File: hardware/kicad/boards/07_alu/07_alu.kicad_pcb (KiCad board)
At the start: 2 copper layers, 104 parts, among them J1 Conn_01x08_Pin, J2 Conn_01x08_Pin, J3 Conn_01x08_Pin, J4 Conn_01x08_Pin, J5 Conn_01x08_Pin, J6 Conn_01x08_Pin, J7 Conn_01x16, SW1 SW_Slide_DPDT, U1 74ACT151, U10 74ACT151, U11 74ACT151, U12 74ACT151, U13 74ACT151, U14 74ACT151, U15 74ACT283, U16 74LS32, U17 74ACT151, U18 74ACT151, U19 74ACT151, U2 74ACT151, U20 74ACT151, U21 74ACT151, U22 74ACT151, U23 74ACT151, U24 74ACT151, U25 74ACT283, U26 74LS32, U27 74ACT151, U28 74ACT151, U29 74ACT151, U3 74ACT283, U30 74ACT151, U31 74ACT151, U32 74ACT151, U33 74ACT151, U34 74ACT151, U35 SST39SF040, U36 SST39SF040, U37 74AHC541, U38 74AHC541, U39 SST39SF040, U4 74LS32, U40 74AHC541, U41 74ACT151, U42 74ACT151, U43 74ACT151, U44 74ACT151, U45 74ACT151, U46 74ACT151, U47 74ACT151, U48 74ACT151, U5 74ACT283, U6 74LS32, U7 74ACT151, U8 74ACT151, U9 74ACT151

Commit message: checkpoint: most recent 16b cell: ~120mm by 120mm
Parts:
- removed C1, C10, C11, C12, C13, C14, C15, C17, C18, C19, C2, C20, C21, C22, C23, C24, C25, C26, C27, C28, C29, C30, C31, C32, C33, C34, C35, C38, C7, C8, C9: 100nF, Capacitor_SMD:C_0603_1608Metric
- removed SW1: SW_Slide_DPDT, Button_Switch_SMD:SW_DPDT_CK_JS202011JCQN
- removed U1, U10, U11, U12, U13, U14, U17, U18, U19, U2, U20, U21, U22, U23, U24, U27, U28, U29, U30, U31, U32, U33, U34, U9: 74ACT151, Package_SO:SOIC-16_3.9x9.9mm_P1.27mm
- removed U15, U25: 74ACT283, Package_SO:SOIC-16_3.9x9.9mm_P1.27mm
- removed U26: 74LS32, Package_SO:SOIC-14_3.9x8.7mm_P1.27mm
- removed U35, U39: SST39SF040, Package_DIP:DIP-32_W15.24mm
- added C49: 100nF, Capacitor_SMD:C_0603_1608Metric, F.Cu at (57.5, 41.8)
- added C50: 100nF, Capacitor_SMD:C_0603_1608Metric, F.Cu at (57.5, 44.3)
- added C51: 100nF, Capacitor_SMD:C_0603_1608Metric, F.Cu at (132.9, 125.5)
- added C52: 100nF, Capacitor_SMD:C_0603_1608Metric, F.Cu at (118.4, 125.5)
- added C53: 100nF, Capacitor_SMD:C_0603_1608Metric, F.Cu at (132.9, 111.8)
- added C54: 100nF, Capacitor_SMD:C_0603_1608Metric, F.Cu at (147.4, 98.2)
- added C55: 100nF, Capacitor_SMD:C_0603_1608Metric, F.Cu at (147.4, 111.8)
- added C56: 100nF, Capacitor_SMD:C_0603_1608Metric, F.Cu at (118.4, 111.8)
- added C57: 100nF, Capacitor_SMD:C_0603_1608Metric, F.Cu at (132.9, 98.2)
- added C58: 100nF, Capacitor_SMD:C_0603_1608Metric, F.Cu at (161.8, 98.2)
- added C59: 100nF, Capacitor_SMD:C_0603_1608Metric, F.Cu at (132.9, 84.6)
- added C60: 100nF, Capacitor_SMD:C_0603_1608Metric, F.Cu at (118.4, 71.0)
- added C61: 100nF, Capacitor_SMD:C_0603_1608Metric, F.Cu at (118.4, 84.6)
- added C62: 100nF, Capacitor_SMD:C_0603_1608Metric, F.Cu at (147.4, 71.0)
- added C63: 100nF, Capacitor_SMD:C_0603_1608Metric, F.Cu at (161.8, 84.6)
- added C64: 100nF, Capacitor_SMD:C_0603_1608Metric, F.Cu at (161.8, 57.4)
- added C65: 100nF, Capacitor_SMD:C_0603_1608Metric, F.Cu at (132.9, 71.0)
- added C66: 100nF, Capacitor_SMD:C_0603_1608Metric, F.Cu at (161.8, 71.0)
- added C67: 100nF, Capacitor_SMD:C_0603_1608Metric, F.Cu at (118.4, 57.4)
- added C68: 100nF, Capacitor_SMD:C_0603_1608Metric, F.Cu at (66.0, 130.8)
- added C69: 100nF, Capacitor_SMD:C_0603_1608Metric, F.Cu at (94.9, 130.8)
- added C70: 100nF, Capacitor_SMD:C_0603_1608Metric, F.Cu at (80.4, 130.8)
- added C71: 100nF, Capacitor_SMD:C_0603_1608Metric, F.Cu at (132.9, 57.4)
- added C72: 100nF, Capacitor_SMD:C_0603_1608Metric, F.Cu at (66.0, 117.2)
- added C73: 100nF, Capacitor_SMD:C_0603_1608Metric, F.Cu at (80.4, 117.2)
- added C74: 100nF, Capacitor_SMD:C_0603_1608Metric, F.Cu at (94.9, 117.2)
- added D1: LED, LED_SMD:LED_0805_2012Metric, F.Cu at (158.8, 29.5)
- added D10: LED, LED_SMD:LED_0805_2012Metric, F.Cu at (57.7, 103.3)
- added D11: LED, LED_SMD:LED_0805_2012Metric, F.Cu at (57.7, 106.4)
- added D12: LED, LED_SMD:LED_0805_2012Metric, F.Cu at (57.7, 109.4)
- added D13: LED, LED_SMD:LED_0805_2012Metric, F.Cu at (57.7, 112.4)
- added D14: LED, LED_SMD:LED_0805_2012Metric, F.Cu at (62.2, 94.2)
- added D15: LED, LED_SMD:LED_0805_2012Metric, F.Cu at (62.2, 97.2)
- added D16: LED, LED_SMD:LED_0805_2012Metric, F.Cu at (62.2, 100.3)
- added D17: LED, LED_SMD:LED_0805_2012Metric, F.Cu at (62.2, 103.3)
- added D18: LED, LED_SMD:LED_0805_2012Metric, F.Cu at (62.2, 106.4)
- added D19: LED, LED_SMD:LED_0805_2012Metric, F.Cu at (62.2, 109.4)
- added D20: LED, LED_SMD:LED_0805_2012Metric, F.Cu at (62.2, 112.4)
- added D21: LED, LED_SMD:LED_0805_2012Metric, F.Cu at (66.6, 94.2)
- added D22: LED, LED_SMD:LED_0805_2012Metric, F.Cu at (66.6, 97.2)
- added D23: LED, LED_SMD:LED_0805_2012Metric, F.Cu at (66.6, 100.3)
- added D24: LED, LED_SMD:LED_0805_2012Metric, F.Cu at (66.6, 103.3)
- added D25: LED, LED_SMD:LED_0805_2012Metric, F.Cu at (66.6, 106.4)
- added D26: LED, LED_SMD:LED_0805_2012Metric, F.Cu at (66.6, 109.4)
- added D27: LED, LED_SMD:LED_0805_2012Metric, F.Cu at (66.6, 112.4)
- added D28: LED, LED_SMD:LED_0805_2012Metric, F.Cu at (71.1, 94.2)
- added D29: LED, LED_SMD:LED_0805_2012Metric, F.Cu at (71.1, 97.2)
- added D3: LED, LED_SMD:LED_0805_2012Metric, F.Cu at (57.7, 94.2)
- added D30: LED, LED_SMD:LED_0805_2012Metric, F.Cu at (71.1, 100.3)
- added D31: LED, LED_SMD:LED_0805_2012Metric, F.Cu at (71.1, 103.3)
- added D32: LED, LED_SMD:LED_0805_2012Metric, F.Cu at (71.1, 106.4)
- added D4: LED, LED_SMD:LED_0805_2012Metric, F.Cu at (57.7, 97.2)
- added D9: LED, LED_SMD:LED_0805_2012Metric, F.Cu at (57.7, 100.3)
- added J10: Conn_01x04_Pin, Connector_PinHeader_2.54mm:PinHeader_1x04_P2.54mm_Vertical, F.Cu at (57.8, 80.8)
- added J11: Conn_01x04_Pin, Connector_PinHeader_2.54mm:PinHeader_1x04_P2.54mm_Vertical, F.Cu at (62.4, 80.8)
- added J12: Conn_01x08_Pin, Connector_PinHeader_2.54mm:PinHeader_1x08_P2.54mm_Vertical, F.Cu at (99.1, 58.4)
- added J13: Conn_01x08_Pin, Connector_PinHeader_2.54mm:PinHeader_1x08_P2.54mm_Vertical, F.Cu at (103.7, 58.4)
- added J8: Conn_01x08_Pin, Connector_PinHeader_2.54mm:PinHeader_1x08_P2.54mm_Vertical, F.Cu at (89.9, 58.4)
- added J9: Conn_01x08_Pin, Connector_PinHeader_2.54mm:PinHeader_1x08_P2.54mm_Vertical, F.Cu at (94.5, 58.4)
- added R1: 330 Ohm, Resistor_SMD:R_0603_1608Metric, F.Cu at (158.5, 32.3)
- added R10: 330, Resistor_SMD:R_0603_1608Metric, F.Cu at (75.3, 101.5)
- added R11: 330, Resistor_SMD:R_0603_1608Metric, F.Cu at (75.3, 104.0)
- added R12: 330, Resistor_SMD:R_0603_1608Metric, F.Cu at (75.3, 106.5)
- added R13: 330, Resistor_SMD:R_0603_1608Metric, F.Cu at (75.3, 109.0)
- added R14: 330, Resistor_SMD:R_0603_1608Metric, F.Cu at (79.3, 93.9)
- added R15: 330, Resistor_SMD:R_0603_1608Metric, F.Cu at (79.3, 96.4)
- added R16: 330, Resistor_SMD:R_0603_1608Metric, F.Cu at (79.3, 99.0)
- added R17: 330, Resistor_SMD:R_0603_1608Metric, F.Cu at (79.3, 101.5)
- added R18: 330, Resistor_SMD:R_0603_1608Metric, F.Cu at (79.3, 104.0)
- added R19: 330, Resistor_SMD:R_0603_1608Metric, F.Cu at (79.3, 106.5)
- added R20: 330, Resistor_SMD:R_0603_1608Metric, F.Cu at (79.3, 109.0)
- added R21: 330, Resistor_SMD:R_0603_1608Metric, F.Cu at (83.3, 93.9)
- added R22: 330, Resistor_SMD:R_0603_1608Metric, F.Cu at (83.3, 96.4)
- added R23: 330, Resistor_SMD:R_0603_1608Metric, F.Cu at (83.3, 99.0)
- added R24: 330, Resistor_SMD:R_0603_1608Metric, F.Cu at (83.3, 101.5)
- added R25: 330, Resistor_SMD:R_0603_1608Metric, F.Cu at (83.3, 104.0)
- added R26: 330, Resistor_SMD:R_0603_1608Metric, F.Cu at (83.3, 106.5)
- added R27: 330, Resistor_SMD:R_0603_1608Metric, F.Cu at (83.3, 109.0)
- added R28: 330, Resistor_SMD:R_0603_1608Metric, F.Cu at (87.3, 93.9)
- added R29: 330, Resistor_SMD:R_0603_1608Metric, F.Cu at (87.3, 96.4)
- added R3: 330 Ohm, Resistor_SMD:R_0603_1608Metric, F.Cu at (75.3, 93.9)
- added R30: 330, Resistor_SMD:R_0603_1608Metric, F.Cu at (87.3, 99.0)
- added R31: 330, Resistor_SMD:R_0603_1608Metric, F.Cu at (87.3, 101.5)
- added R4: 330, Resistor_SMD:R_0603_1608Metric, F.Cu at (75.3, 96.4)
- added R9: 330, Resistor_SMD:R_0603_1608Metric, F.Cu at (75.3, 99.0)
- added U49: 74ACT151, Package_SO:SOIC-16_3.9x9.9mm_P1.27mm, F.Cu at (141.1, 102.9)
- added U50: 74ACT151, Package_SO:SOIC-16_3.9x9.9mm_P1.27mm, F.Cu at (126.7, 130.1)
- added U51: 74ACT151, Package_SO:SOIC-16_3.9x9.9mm_P1.27mm, F.Cu at (112.2, 130.1)
- added U52: 74ACT151, Package_SO:SOIC-16_3.9x9.9mm_P1.27mm, F.Cu at (126.7, 116.5)
- added U53: 74ACT151, Package_SO:SOIC-16_3.9x9.9mm_P1.27mm, F.Cu at (141.1, 116.5)
- added U54: 74ACT151, Package_SO:SOIC-16_3.9x9.9mm_P1.27mm, F.Cu at (126.7, 102.9)
- added U55: 74ACT151, Package_SO:SOIC-16_3.9x9.9mm_P1.27mm, F.Cu at (155.6, 102.9)
- added U56: 74ACT151, Package_SO:SOIC-16_3.9x9.9mm_P1.27mm, F.Cu at (112.2, 116.5)
- added U57: 74ACT151, Package_SO:SOIC-16_3.9x9.9mm_P1.27mm, F.Cu at (141.1, 75.6)
- added U58: 74ACT151, Package_SO:SOIC-16_3.9x9.9mm_P1.27mm, F.Cu at (126.7, 89.2)
- added U59: 74ACT151, Package_SO:SOIC-16_3.9x9.9mm_P1.27mm, F.Cu at (112.2, 75.6)
- added U60: 74ACT151, Package_SO:SOIC-16_3.9x9.9mm_P1.27mm, F.Cu at (112.2, 89.2)
- added U61: 74ACT151, Package_SO:SOIC-16_3.9x9.9mm_P1.27mm, F.Cu at (155.6, 89.2)
- added U62: 74ACT151, Package_SO:SOIC-16_3.9x9.9mm_P1.27mm, F.Cu at (126.7, 75.6)
- added U63: 74ACT151, Package_SO:SOIC-16_3.9x9.9mm_P1.27mm, F.Cu at (155.6, 75.6)
- added U64: 74ACT151, Package_SO:SOIC-16_3.9x9.9mm_P1.27mm, F.Cu at (155.6, 62.0)
- added U65: 74ACT151, Package_SO:SOIC-16_3.9x9.9mm_P1.27mm, F.Cu at (74.2, 135.5)
- added U66: 74ACT151, Package_SO:SOIC-16_3.9x9.9mm_P1.27mm, F.Cu at (112.2, 62.0)
- added U67: 74ACT151, Package_SO:SOIC-16_3.9x9.9mm_P1.27mm, F.Cu at (59.7, 135.5)
- added U68: 74ACT151, Package_SO:SOIC-16_3.9x9.9mm_P1.27mm, F.Cu at (88.6, 135.5)
- added U69: 74ACT151, Package_SO:SOIC-16_3.9x9.9mm_P1.27mm, F.Cu at (126.7, 62.0)
- added U70: 74ACT151, Package_SO:SOIC-16_3.9x9.9mm_P1.27mm, F.Cu at (74.2, 121.9)
- added U71: 74ACT151, Package_SO:SOIC-16_3.9x9.9mm_P1.27mm, F.Cu at (88.6, 121.9)
- added U72: 74ACT151, Package_SO:SOIC-16_3.9x9.9mm_P1.27mm, F.Cu at (59.7, 121.9)
- J7: value Conn_01x16 -> Conn_01x08_Pin; footprint Connector_PinHeader_2.54mm:PinHeader_1x16_P2.54mm_Vertical -> Connector_PinHeader_2.54mm:PinHeader_1x08_P2.54mm_Vertical
- U16: value 74LS32 -> 74ACT151; footprint Package_SO:SOIC-14_3.9x8.7mm_P1.27mm -> Package_SO:SOIC-16_3.9x9.9mm_P1.27mm
- U36: value SST39SF040 -> 74HC86; footprint Package_DIP:DIP-32_W15.24mm -> Package_SO:SOIC-14_3.9x8.7mm_P1.27mm
- U37: value 74AHC541 -> 74LS08; footprint Package_SO:SOIC-20W_7.5x12.8mm_P1.27mm -> Package_SO:SOIC-14_3.9x8.7mm_P1.27mm
- U38: value 74AHC541 -> 74LS540
- U4, U6: value 74LS32 -> 74HC688; footprint Package_SO:SOIC-14_3.9x8.7mm_P1.27mm -> Package_SO:SOIC-20W_7.5x12.8mm_P1.27mm
- U40: value 74AHC541 -> 74LS377
- U7, U8: value 74ACT151 -> 74ACT283
- moved U4 100.0 mm to (66.0, 35.3)
- moved C44 91.6 mm to (138.1, 29.3)
- moved C45 91.6 mm to (152.5, 29.3)
- moved C47 91.6 mm to (138.1, 42.9)
- moved U44 91.6 mm to (131.8, 33.9)
- moved U45 91.6 mm to (146.3, 33.9)
- moved U47 91.6 mm to (131.8, 47.5)
- moved C16 87.5 mm to (57.5, 29.3)
- moved U43 82.0 mm to (117.4, 33.9)
- moved C43 82.0 mm to (123.6, 29.3)
- moved U6 80.1 mm to (78.9, 35.3)
- moved C48 76.5 mm to (123.6, 42.9)
- moved U48 76.5 mm to (117.4, 47.5)
- moved U5 75.4 mm to (112.2, 102.9)
- moved C6 72.8 mm to (101.8, 93.9)
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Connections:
- C36 pad 1: VCC -> GND
- C36 pad 2: GND -> VCC
- C37 pad 1: VCC -> GND
- C37 pad 2: GND -> VCC
- C39 pad 1: VCC -> GND
- C39 pad 2: GND -> VCC
- J7 pad 1: OPCODE0 -> ALU_OPCODE_Y0
- J7 pad 2: OPCODE1 -> ALU_OPCODE_Y1
- J7 pad 3: OPCODE2 -> ALU_OPCODE_Y2
- J7 pad 4: OPCODE3 -> ALU_OPCODE_Y3
- J7 pad 5: OPCODE4 -> ALU_OPCODE_Y4
- J7 pad 6: OPCODE5 -> ALU_OPCODE_Y5
- J7 pad 7: OPCODE6 -> ALU_OPCODE_Y6
- J7 pad 8: OPCODE7 -> ALU_OPCODE_Y7
- U16 pad 1: OUT8 -> flagZ
- U16 pad 10: Net-(U16-Pad10) -> CSEL1
- U16 pad 11: /alu_4b_2/Z_out -> CSEL0
- U16 pad 12: Net-(U16-Pad12) -> flagGT
- U16 pad 13: /alu_4b_1/Z_out -> flagLT
- U16 pad 14: VCC -> flagV
- U16 pad 2: OUT9 -> flagC
- U16 pad 3: Net-(U16-Pad3) -> VCC
- U16 pad 4: OUT10 -> GND
- U16 pad 5: OUT11 -> CIN-MAIN
- U16 pad 6: Net-(U16-Pad10) -> unconnected-(U16-~{Z}-Pad6)
- U16 pad 8: Net-(U16-Pad12) -> GND
- U16 pad 9: Net-(U16-Pad3) -> CSEL2
- U3 pad 7: CIN -> CIN-MAIN
- U36 pad 1: GND -> Aeff
- U36 pad 10: OPCODE2 -> VOUT
- U36 pad 11: OPCODE1 -> unconnected-(U36-Pad11)
- U36 pad 12: OPCODE0 -> unconnected-(U36-Pad12)
- U36 pad 13: Net-(U36-D0) -> unconnected-(U36-Pad13)
- U36 pad 14: Net-(U36-D1) -> VCC
- U36 pad 2: GND -> sum15
- U36 pad 3: OPCODE15 -> Net-(U36-Pad3)
- U36 pad 4: OPCODE12 -> sum15
- U36 pad 5: OPCODE7 -> Beff
- U36 pad 6: OPCODE6 -> Net-(U36-Pad6)
- U36 pad 7: OPCODE5 -> GND
- U36 pad 8: OPCODE4 -> LT-SIGN
- U36 pad 9: OPCODE3 -> OUT15
- U37 pad 1: GND -> Net-(U36-Pad3)
- U37 pad 10: GND -> unconnected-(U37-Pad10)
- U37 pad 11: CTRL2 -> GT-SIGN
- U37 pad 12: CTRL1 -> GTE-SIGN
- U37 pad 13: CTRL0 -> ~ZOUT
- U37 pad 14: FLAG_WE -> VCC
- U37 pad 2: Net-(U36-D0) -> Net-(U36-Pad6)
- U37 pad 3: Net-(U36-D1) -> VOUT
- U37 pad 4: Net-(U36-D2) -> unconnected-(U37-Pad4)
- U37 pad 5: Net-(U36-D3) -> unconnected-(U37-Pad5)
- U37 pad 6: Net-(U36-D4) -> unconnected-(U37-Pad6)
- U37 pad 7: Net-(U36-D5) -> GND
- U37 pad 8: Net-(U36-D6) -> unconnected-(U37-Pad8)
- U37 pad 9: Net-(U36-D7) -> unconnected-(U37-Pad9)
- U38 pad 11: ALU_OPCODE_X7 -> unconnected-(U38-Y7-Pad11)
- U38 pad 12: ALU_OPCODE_X6 -> unconnected-(U38-Y6-Pad12)
- U38 pad 13: ALU_OPCODE_X5 -> ~flagWE
- U38 pad 14: ALU_OPCODE_X4 -> unconnected-(U38-Y4-Pad14)
- U38 pad 15: ALU_OPCODE_X3 -> GTE-SIGN
- U38 pad 16: ALU_OPCODE_X2 -> unconnected-(U38-Y2-Pad16)
- U38 pad 17: ALU_OPCODE_X1 -> unconnected-(U38-Y1-Pad17)
- U38 pad 18: ALU_OPCODE_X0 -> ZOUT
- U38 pad 2: Net-(U35-D0) -> ~ZOUT
- U38 pad 3: Net-(U35-D1) -> unconnected-(U38-A1-Pad3)
- U38 pad 4: Net-(U35-D2) -> VOUT
- U38 pad 5: Net-(U35-D3) -> LT-SIGN
- U38 pad 6: Net-(U35-D4) -> OUT15
- U38 pad 7: Net-(U35-D5) -> FLAG_WE
- U38 pad 8: Net-(U35-D6) -> unconnected-(U38-A6-Pad8)
- U38 pad 9: Net-(U35-D7) -> unconnected-(U38-A7-Pad9)
- U4 pad 1: OUT0 -> GND
- U4 pad 10: Net-(U4-Pad10) -> GND
- U4 pad 11: /alu_4b_0/Z_out -> OUT4
- U4 pad 12: Net-(U4-Pad12) -> GND
- U4 pad 13: /alu_4b_0/Z_in -> OUT5
- U4 pad 14: VCC -> GND
- U4 pad 2: OUT1 -> OUT0
- U4 pad 3: Net-(U4-Pad3) -> GND
- U4 pad 4: OUT2 -> OUT1
- U4 pad 5: OUT3 -> GND
- U4 pad 6: Net-(U4-Pad10) -> OUT2
- U4 pad 8: Net-(U4-Pad12) -> OUT3
- U4 pad 9: Net-(U4-Pad3) -> GND
- U40 pad 1: GND -> ~flagWE
- U40 pad 11: ALU_OPCODE_Y7 -> SYS-CLK
- U40 pad 12: ALU_OPCODE_Y6 -> flagV
- U40 pad 13: ALU_OPCODE_Y5 -> VOUT
- U40 pad 14: ALU_OPCODE_Y4 -> LT-SIGN
- U40 pad 15: ALU_OPCODE_Y3 -> flagLT
- U40 pad 16: ALU_OPCODE_Y2 -> flagGT
- U40 pad 17: ALU_OPCODE_Y1 -> GT-SIGN
- U40 pad 18: ALU_OPCODE_Y0 -> GTE-SIGN
- U40 pad 19: GND -> flagGTE
- U40 pad 2: Net-(U39-D0) -> flagZ
- U40 pad 3: Net-(U39-D1) -> ZOUT
- U40 pad 4: Net-(U39-D2) -> ~ZOUT
- U40 pad 5: Net-(U39-D3) -> ~flagZ
- U40 pad 6: Net-(U39-D4) -> flagN
- U40 pad 7: Net-(U39-D5) -> OUT15
- U40 pad 8: Net-(U39-D6) -> COUT-MAIN
- U40 pad 9: Net-(U39-D7) -> flagC
- U6 pad 1: OUT4 -> Net-(U4-P=R)
- U6 pad 10: Net-(U6-Pad10) -> GND
- U6 pad 11: /alu_4b_1/Z_out -> OUT12
- U6 pad 12: Net-(U6-Pad12) -> GND
- U6 pad 13: /alu_4b_0/Z_out -> OUT13
- U6 pad 14: VCC -> GND
- U6 pad 2: OUT5 -> OUT8
- U6 pad 3: Net-(U6-Pad3) -> GND
- U6 pad 4: OUT6 -> OUT9
- U6 pad 5: OUT7 -> GND
- U6 pad 6: Net-(U6-Pad10) -> OUT10
- U6 pad 8: Net-(U6-Pad12) -> OUT11
- U6 pad 9: Net-(U6-Pad3) -> GND
- U7 pad 1: ALU_OPCODE_X3 -> OUT9
- U7 pad 10: B4 -> OUT11
- U7 pad 11: A4 -> /alu_4b_2/logB3
- U7 pad 12: ALU_OPCODE_X7 -> /alu_4b_2/logA3
- U7 pad 13: ALU_OPCODE_X6 -> OUT10
- U7 pad 14: ALU_OPCODE_X5 -> /alu_4b_2/logA2
- U7 pad 15: ALU_OPCODE_X4 -> /alu_4b_2/logB2
- U7 pad 2: ALU_OPCODE_X2 -> /alu_4b_2/logB1
- U7 pad 3: ALU_OPCODE_X1 -> /alu_4b_2/logA1
- U7 pad 4: ALU_OPCODE_X0 -> OUT8
- U7 pad 5: /alu_4b_1/logA0 -> /alu_4b_2/logA0
- U7 pad 6: unconnected-(U7-~{Z}-Pad6) -> /alu_4b_2/logB0
- U7 pad 7: GND -> /alu_4b_1/cout
- U7 pad 9: C4 -> /alu_4b_2/cout
- U8 pad 1: ALU_OPCODE_X3 -> OUT13
- U8 pad 10: B5 -> sum15
- U8 pad 11: A5 -> Beff
- U8 pad 12: ALU_OPCODE_X7 -> Aeff
- U8 pad 13: ALU_OPCODE_X6 -> OUT14
- U8 pad 14: ALU_OPCODE_X5 -> /alu_4b_3/logA2
- U8 pad 15: ALU_OPCODE_X4 -> /alu_4b_3/logB2
- U8 pad 2: ALU_OPCODE_X2 -> /alu_4b_3/logB1
- U8 pad 3: ALU_OPCODE_X1 -> /alu_4b_3/logA1
- U8 pad 4: ALU_OPCODE_X0 -> OUT12
- U8 pad 5: /alu_4b_1/logA1 -> /alu_4b_3/logA0
- U8 pad 6: unconnected-(U8-~{Z}-Pad6) -> /alu_4b_3/logB0
- U8 pad 7: GND -> /alu_4b_2/cout
- U8 pad 9: C5 -> COUT-MAIN

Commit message: feat: placed components in 16b cell
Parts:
- removed C16, C36, C37, C39, C4, C40, C49, C5, C50, C51, C52, C53, C54, C55, C56, C57, C58, C59, C6, C60, C61, C62, C63, C64, C65, C66, C67, C68, C69, C70, C71, C72, C73, C74: 100nF, Capacitor_SMD:C_0603_1608Metric
- removed D1, D10, D11, D12, D13, D14, D15, D16, D17, D18, D19, D20, D21, D22, D23, D24, D25, D26, D27, D28, D29, D3, D30, D31, D32, D4, D9: LED, LED_SMD:LED_0805_2012Metric
- removed J1, J12, J13, J2, J3, J4, J5, J6, J7, J8, J9: Conn_01x08_Pin, Connector_PinHeader_2.54mm:PinHeader_1x08_P2.54mm_Vertical
- removed J10, J11: Conn_01x04_Pin, Connector_PinHeader_2.54mm:PinHeader_1x04_P2.54mm_Vertical
- removed R1, R3: 330 Ohm, Resistor_SMD:R_0603_1608Metric
- removed R10, R11, R12, R13, R14, R15, R16, R17, R18, R19, R20, R21, R22, R23, R24, R25, R26, R27, R28, R29, R30, R31, R4, R9: 330, Resistor_SMD:R_0603_1608Metric
- removed U16, U49, U50, U51, U52, U53, U54, U55, U56, U57, U58, U59, U60, U61, U62, U63, U64, U65, U66, U67, U68, U69, U70, U71, U72: 74ACT151, Package_SO:SOIC-16_3.9x9.9mm_P1.27mm
- removed U36: 74HC86, Package_SO:SOIC-14_3.9x8.7mm_P1.27mm
- removed U37: 74LS08, Package_SO:SOIC-14_3.9x8.7mm_P1.27mm
- removed U38: 74LS540, Package_SO:SOIC-20W_7.5x12.8mm_P1.27mm
- removed U4, U6: 74HC688, Package_SO:SOIC-20W_7.5x12.8mm_P1.27mm
- removed U40: 74LS377, Package_SO:SOIC-20W_7.5x12.8mm_P1.27mm
- removed U5, U7, U8: 74ACT283, Package_SO:SOIC-16_3.9x9.9mm_P1.27mm
- moved C48 204.2 mm to (305.2, 136.2)
- moved C47 184.2 mm to (305.2, 120.4)
- moved U48 180.1 mm to (274.5, 135.5)
- moved U43 164.9 mm to (255.0, 124.7)
- moved C45 164.4 mm to (304.8, 91.2)
- moved U47 162.2 mm to (274.5, 124.7)
- moved U44 159.7 mm to (255.0, 135.5)
- moved U45 145.7 mm to (274.5, 103.1)
- moved C46 144.8 mm to (305.2, 105.4)
- moved C43 123.4 mm to (211.0, 116.4)
- moved C44 123.4 mm to (211.0, 128.8)
- moved U46 120.0 mm to (274.5, 113.9)
- moved C3 116.2 mm to (276.2, 91.8)
- moved U42 115.0 mm to (255.0, 113.9)
- moved U41 114.7 mm to (255.0, 103.1)
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
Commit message: fix: resolved kicad erc tests to 0
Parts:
- added C16: 100nF, Capacitor_SMD:C_0603_1608Metric, F.Cu at (71.4, 112.1)
- added C36: 100nF, Capacitor_SMD:C_0603_1608Metric, F.Cu at (90.7, 119.3)
- added C37: 100nF, Capacitor_SMD:C_0603_1608Metric, F.Cu at (106.7, 119.5)
- added C39: 100nF, Capacitor_SMD:C_0603_1608Metric, F.Cu at (117.2, 121.3)
- added C4: 100nF, Capacitor_SMD:C_0603_1608Metric, F.Cu at (134.6, 78.8)
- added C40: 100nF, Capacitor_SMD:C_0603_1608Metric, F.Cu at (125.7, 121.6)
- added C49: 100nF, Capacitor_SMD:C_0603_1608Metric, F.Cu at (134.2, 121.1)
- added C51: 100nF, Capacitor_SMD:C_0603_1608Metric, F.Cu at (120.2, 97.9)
- added C52: 100nF, Capacitor_SMD:C_0603_1608Metric, F.Cu at (120.2, 61.9)
- added C53: 100nF, Capacitor_SMD:C_0603_1608Metric, F.Cu at (119.9, 73.9)
- added C54: 100nF, Capacitor_SMD:C_0603_1608Metric, F.Cu at (120.2, 85.9)
- added C55: 100nF, Capacitor_SMD:C_0603_1608Metric, F.Cu at (147.0, 96.8)
- added C56: 100nF, Capacitor_SMD:C_0603_1608Metric, F.Cu at (147.2, 60.8)
- added C57: 100nF, Capacitor_SMD:C_0603_1608Metric, F.Cu at (147.0, 72.8)
- added C58: 100nF, Capacitor_SMD:C_0603_1608Metric, F.Cu at (147.0, 84.8)
- added D10: LED, LED_SMD:LED_0805_2012Metric, F.Cu at (56.3, 133.0)
- added D11: LED, LED_SMD:LED_0805_2012Metric, F.Cu at (59.4, 133.0)
- added D12: LED, LED_SMD:LED_0805_2012Metric, F.Cu at (62.4, 133.0)
- added D13: LED, LED_SMD:LED_0805_2012Metric, F.Cu at (65.4, 133.0)
- added D14: LED, LED_SMD:LED_0805_2012Metric, F.Cu at (67.7, 132.9)
- added D15: LED, LED_SMD:LED_0805_2012Metric, F.Cu at (69.9, 132.7)
- added D16: LED, LED_SMD:LED_0805_2012Metric, F.Cu at (59.3, 57.6)
- added D17: LED, LED_SMD:LED_0805_2012Metric, F.Cu at (59.3, 67.4)
- added D18: LED, LED_SMD:LED_0805_2012Metric, F.Cu at (59.3, 70.0)
- added D19: LED, LED_SMD:LED_0805_2012Metric, F.Cu at (59.3, 72.6)
- added D20: LED, LED_SMD:LED_0805_2012Metric, F.Cu at (59.3, 75.2)
- added D21: LED, LED_SMD:LED_0805_2012Metric, F.Cu at (59.3, 77.7)
- added D22: LED, LED_SMD:LED_0805_2012Metric, F.Cu at (59.3, 80.3)
- added D23: LED, LED_SMD:LED_0805_2012Metric, F.Cu at (59.3, 82.9)
- added D24: LED, LED_SMD:LED_0805_2012Metric, F.Cu at (59.3, 85.5)
- added D25: LED, LED_SMD:LED_0805_2012Metric, F.Cu at (58.8, 91.1)
- added D26: LED, LED_SMD:LED_0805_2012Metric, F.Cu at (58.8, 93.6)
- added D27: LED, LED_SMD:LED_0805_2012Metric, F.Cu at (58.8, 96.2)
- added D28: LED, LED_SMD:LED_0805_2012Metric, F.Cu at (58.8, 98.8)
- added D29: LED, LED_SMD:LED_0805_2012Metric, F.Cu at (58.8, 101.4)
- added D3: LED, LED_SMD:LED_0805_2012Metric, F.Cu at (139.7, 47.1)
- added D30: LED, LED_SMD:LED_0805_2012Metric, F.Cu at (58.8, 103.9)
- added D31: LED, LED_SMD:LED_0805_2012Metric, F.Cu at (58.8, 106.5)
- added D32: LED, LED_SMD:LED_0805_2012Metric, F.Cu at (58.8, 109.1)
- added D33: LED, LED_SMD:LED_0805_2012Metric, F.Cu at (142.2, 47.0)
- added D34: LED, LED_SMD:LED_0805_2012Metric, F.Cu at (59.3, 60.2)
- added D35: LED, LED_SMD:LED_0805_2012Metric, F.Cu at (59.3, 62.7)
- added D36: LED, LED_SMD:LED_0805_2012Metric, F.Cu at (89.0, 56.8)
- added D37: LED, LED_SMD:LED_0805_2012Metric, F.Cu at (86.8, 56.9)
- added D38: LED, LED_SMD:LED_0805_2012Metric, F.Cu at (84.7, 56.9)
- added D39: LED, LED_SMD:LED_0805_2012Metric, F.Cu at (82.5, 56.9)
- added D4: LED, LED_SMD:LED_0805_2012Metric, F.Cu at (75.4, 132.5)
- added D40: LED, LED_SMD:LED_0805_2012Metric, F.Cu at (80.5, 57.1)
- added D41: LED, LED_SMD:LED_0805_2012Metric, F.Cu at (78.3, 57.1)
- added D42: LED, LED_SMD:LED_0805_2012Metric, F.Cu at (76.2, 57.0)
- added D43: LED, LED_SMD:LED_0805_2012Metric, F.Cu at (74.0, 57.0)
- added D44: LED, LED_SMD:LED_0805_2012Metric, F.Cu at (113.0, 56.2)
- added D45: LED, LED_SMD:LED_0805_2012Metric, F.Cu at (110.8, 56.2)
- added D46: LED, LED_SMD:LED_0805_2012Metric, F.Cu at (108.7, 56.3)
- added D47: LED, LED_SMD:LED_0805_2012Metric, F.Cu at (106.5, 56.3)
- added D48: LED, LED_SMD:LED_0805_2012Metric, F.Cu at (104.5, 56.1)
- added D49: LED, LED_SMD:LED_0805_2012Metric, F.Cu at (102.5, 56.0)
- added D5: LED, LED_SMD:LED_0805_2012Metric, F.Cu at (59.3, 55.0)
- added D50: LED, LED_SMD:LED_0805_2012Metric, F.Cu at (100.3, 56.0)
- added D51: LED, LED_SMD:LED_0805_2012Metric, F.Cu at (98.3, 56.0)
- added D52: LED, LED_SMD:LED_0805_2012Metric, F.Cu at (134.9, 57.5)
- added D53: LED, LED_SMD:LED_0805_2012Metric, F.Cu at (132.8, 57.5)
- added D54: LED, LED_SMD:LED_0805_2012Metric, F.Cu at (130.8, 57.6)
- added D55: LED, LED_SMD:LED_0805_2012Metric, F.Cu at (128.8, 57.5)
- added D56: LED, LED_SMD:LED_0805_2012Metric, F.Cu at (126.7, 57.5)
- added D57: LED, LED_SMD:LED_0805_2012Metric, F.Cu at (124.5, 57.6)
- added D58: LED, LED_SMD:LED_0805_2012Metric, F.Cu at (122.5, 57.6)
- added D59: LED, LED_SMD:LED_0805_2012Metric, F.Cu at (120.2, 57.7)
- added D6: LED, LED_SMD:LED_0805_2012Metric, F.Cu at (148.0, 47.0)
- added D60: LED, LED_SMD:LED_0805_2012Metric, F.Cu at (149.2, 130.0)
- added D61: LED, LED_SMD:LED_0805_2012Metric, F.Cu at (149.2, 127.0)
- added D62: LED, LED_SMD:LED_0805_2012Metric, F.Cu at (149.2, 124.0)
- added D63: LED, LED_SMD:LED_0805_2012Metric, F.Cu at (149.2, 120.9)
- added D64: LED, LED_SMD:LED_0805_2012Metric, F.Cu at (149.2, 117.9)
- added D65: LED, LED_SMD:LED_0805_2012Metric, F.Cu at (149.2, 114.8)
- added D66: LED, LED_SMD:LED_0805_2012Metric, F.Cu at (149.2, 111.8)
- added D67: LED, LED_SMD:LED_0805_2012Metric, F.Cu at (149.2, 108.8)
- added D7: LED, LED_SMD:LED_0805_2012Metric, F.Cu at (145.0, 46.9)
- added D9: LED, LED_SMD:LED_0805_2012Metric, F.Cu at (72.2, 132.9)
- added J10: Conn_01x04_Pin, Connector_PinHeader_2.54mm:PinHeader_1x04_P2.54mm_Vertical, F.Cu at (66.2, 55.1)
- added J11: Conn_01x04_Pin, Connector_PinHeader_2.54mm:PinHeader_1x04_P2.54mm_Vertical, F.Cu at (139.4, 56.0)
- added J12: Conn_01x08_Pin, Connector_PinHeader_2.54mm:PinHeader_1x08_P2.54mm_Vertical, F.Cu at (140.4, 128.9)
- added J15: Conn_01x08_Pin, Connector_PinHeader_2.54mm:PinHeader_1x08_P2.54mm_Vertical, F.Cu at (67.0, 91.9)
- added J16: Conn_01x08_Pin, Connector_PinHeader_2.54mm:PinHeader_1x08_P2.54mm_Vertical, F.Cu at (67.6, 67.7)
- added J17: Conn_01x08_Pin, Connector_PinHeader_2.54mm:PinHeader_1x08_P2.54mm_Vertical, F.Cu at (134.6, 135.6)
- added J5: Conn_01x08_Pin, Connector_PinHeader_2.54mm:PinHeader_1x08_P2.54mm_Vertical, F.Cu at (136.1, 47.2)
- added J6: Conn_01x08_Pin, Connector_PinHeader_2.54mm:PinHeader_1x08_P2.54mm_Vertical, F.Cu at (113.5, 46.9)
- added J7: Conn_01x08_Pin, Connector_PinHeader_2.54mm:PinHeader_1x08_P2.54mm_Vertical, F.Cu at (90.6, 47.1)
- added R10: 330, Resistor_SMD:R_0603_1608Metric, F.Cu at (56.4, 129.5)
- added R11: 330, Resistor_SMD:R_0603_1608Metric, F.Cu at (59.4, 129.2)
- added R12: 330, Resistor_SMD:R_0603_1608Metric, F.Cu at (62.4, 129.2)
- added R13: 330, Resistor_SMD:R_0603_1608Metric, F.Cu at (65.2, 129.0)
- added R14: 330, Resistor_SMD:R_0603_1608Metric, F.Cu at (67.7, 129.2)
- added R15: 330, Resistor_SMD:R_0603_1608Metric, F.Cu at (69.4, 129.2)
- added R16: 330, Resistor_SMD:R_0603_1608Metric, F.Cu at (62.6, 67.4)
- added R17: 330, Resistor_SMD:R_0603_1608Metric, F.Cu at (62.6, 70.0)
- added R18: 330, Resistor_SMD:R_0603_1608Metric, F.Cu at (62.6, 72.6)
- added R19: 330, Resistor_SMD:R_0603_1608Metric, F.Cu at (62.6, 75.1)
- added R20: 330, Resistor_SMD:R_0603_1608Metric, F.Cu at (62.6, 77.7)
- added R21: 330, Resistor_SMD:R_0603_1608Metric, F.Cu at (62.6, 80.3)
- added R22: 330, Resistor_SMD:R_0603_1608Metric, F.Cu at (62.6, 82.9)
- added R23: 330, Resistor_SMD:R_0603_1608Metric, F.Cu at (62.6, 85.4)
- added R24: 330, Resistor_SMD:R_0603_1608Metric, F.Cu at (62.0, 91.2)
- added R25: 330, Resistor_SMD:R_0603_1608Metric, F.Cu at (62.0, 93.7)
- added R26: 330, Resistor_SMD:R_0603_1608Metric, F.Cu at (62.0, 96.2)
- added R27: 330, Resistor_SMD:R_0603_1608Metric, F.Cu at (62.0, 98.8)
- added R28: 330, Resistor_SMD:R_0603_1608Metric, F.Cu at (62.0, 101.3)
- added R29: 330, Resistor_SMD:R_0603_1608Metric, F.Cu at (62.0, 103.8)
- added R3: 330 Ohm, Resistor_SMD:R_0603_1608Metric, F.Cu at (139.8, 50.9)
- added R30: 330, Resistor_SMD:R_0603_1608Metric, F.Cu at (62.0, 106.3)
- added R31: 330, Resistor_SMD:R_0603_1608Metric, F.Cu at (62.0, 108.9)
- added R32: 330 Ohm, Resistor_SMD:R_0603_1608Metric, F.Cu at (147.5, 51.5)
- added R33: 330 Ohm, Resistor_SMD:R_0603_1608Metric, F.Cu at (144.8, 51.2)
- added R34: 330 Ohm, Resistor_SMD:R_0603_1608Metric, F.Cu at (62.5, 62.7)
- added R35: 330, Resistor_SMD:R_0603_1608Metric, F.Cu at (87.5, 53.4)
- added R36: 330, Resistor_SMD:R_0603_1608Metric, F.Cu at (85.8, 53.4)
- added R37: 330, Resistor_SMD:R_0603_1608Metric, F.Cu at (84.2, 53.4)
- added R38: 330, Resistor_SMD:R_0603_1608Metric, F.Cu at (82.5, 53.4)
- added R39: 330, Resistor_SMD:R_0603_1608Metric, F.Cu at (80.8, 53.4)
- added R4: 330, Resistor_SMD:R_0603_1608Metric, F.Cu at (75.4, 129.0)
- added R40: 330, Resistor_SMD:R_0603_1608Metric, F.Cu at (79.2, 53.5)
- added R41: 330, Resistor_SMD:R_0603_1608Metric, F.Cu at (77.5, 53.5)
- added R42: 330, Resistor_SMD:R_0603_1608Metric, F.Cu at (75.7, 53.4)
- added R43: 330, Resistor_SMD:R_0603_1608Metric, F.Cu at (110.2, 52.4)
- added R44: 330, Resistor_SMD:R_0603_1608Metric, F.Cu at (108.5, 52.5)
- added R45: 330, Resistor_SMD:R_0603_1608Metric, F.Cu at (106.8, 52.5)
- added R46: 330, Resistor_SMD:R_0603_1608Metric, F.Cu at (105.2, 52.5)
- added R47: 330, Resistor_SMD:R_0603_1608Metric, F.Cu at (103.6, 52.5)
- added R48: 330, Resistor_SMD:R_0603_1608Metric, F.Cu at (102.0, 52.4)
- added R49: 330, Resistor_SMD:R_0603_1608Metric, F.Cu at (100.2, 52.4)
- added R5: 330 Ohm, Resistor_SMD:R_0603_1608Metric, F.Cu at (62.6, 55.0)
- added R50: 330, Resistor_SMD:R_0603_1608Metric, F.Cu at (98.5, 52.5)
- added R51: 330, Resistor_SMD:R_0603_1608Metric, F.Cu at (133.3, 53.7)
- added R52: 330, Resistor_SMD:R_0603_1608Metric, F.Cu at (131.8, 53.7)
- added R53: 330, Resistor_SMD:R_0603_1608Metric, F.Cu at (130.2, 53.8)
- added R54: 330, Resistor_SMD:R_0603_1608Metric, F.Cu at (128.6, 53.8)
- added R55: 330, Resistor_SMD:R_0603_1608Metric, F.Cu at (127.0, 53.8)
- added R56: 330, Resistor_SMD:R_0603_1608Metric, F.Cu at (125.3, 53.8)
- added R57: 330, Resistor_SMD:R_0603_1608Metric, F.Cu at (123.8, 53.8)
- added R58: 330, Resistor_SMD:R_0603_1608Metric, F.Cu at (122.2, 53.8)
- added R59: 330, Resistor_SMD:R_0603_1608Metric, F.Cu at (145.3, 130.1)
- added R6: 330 Ohm, Resistor_SMD:R_0603_1608Metric, F.Cu at (62.6, 57.6)
- added R60: 330, Resistor_SMD:R_0603_1608Metric, F.Cu at (145.4, 126.9)
- added R61: 330, Resistor_SMD:R_0603_1608Metric, F.Cu at (145.5, 123.9)
- added R62: 330, Resistor_SMD:R_0603_1608Metric, F.Cu at (145.4, 121.0)
- added R63: 330, Resistor_SMD:R_0603_1608Metric, F.Cu at (145.6, 117.8)
- added R64: 330, Resistor_SMD:R_0603_1608Metric, F.Cu at (145.7, 114.8)
- added R65: 330, Resistor_SMD:R_0603_1608Metric, F.Cu at (145.5, 111.9)
- added R66: 330, Resistor_SMD:R_0603_1608Metric, F.Cu at (145.4, 108.9)
- added R7: 330 Ohm, Resistor_SMD:R_0603_1608Metric, F.Cu at (142.0, 51.0)
- added R8: 330 Ohm, Resistor_SMD:R_0603_1608Metric, F.Cu at (62.5, 60.2)
- added R9: 330, Resistor_SMD:R_0603_1608Metric, F.Cu at (72.2, 129.4)
- added U16: 74ACT151, Package_SO:SOIC-16_3.9x9.9mm_P1.27mm, F.Cu at (115.2, 127.5)
- added U36: 74HC86, Package_SO:SOIC-14_3.9x8.7mm_P1.27mm, F.Cu at (123.7, 126.8)
- added U37: 74LS08, Package_SO:SOIC-14_3.9x8.7mm_P1.27mm, F.Cu at (132.2, 126.8)
- added U38: 74LS540, Package_SO:SOIC-20W_7.5x12.8mm_P1.27mm, F.Cu at (86.5, 126.8)
- added U4: 74HC688, Package_SO:SOIC-20W_7.5x12.8mm_P1.27mm, F.Cu at (102.5, 127.5)
- added U40: 74LS377, Package_SO:SOIC-20W_7.5x12.8mm_P1.27mm, F.Cu at (65.9, 120.1)
- added U49: 74ACT151, Package_SO:SOIC-16_3.9x9.9mm_P1.27mm, F.Cu at (117.8, 91.9)
- added U5: 74ACT283, Package_SO:SOIC-16_3.9x9.9mm_P1.27mm, F.Cu at (132.4, 85.0)
- added U50: 74ACT151, Package_SO:SOIC-16_3.9x9.9mm_P1.27mm, F.Cu at (117.7, 103.9)
- added U51: 74ACT151, Package_SO:SOIC-16_3.9x9.9mm_P1.27mm, F.Cu at (117.9, 67.9)
- added U52: 74ACT151, Package_SO:SOIC-16_3.9x9.9mm_P1.27mm, F.Cu at (117.9, 79.9)
- added U53: 74ACT151, Package_SO:SOIC-16_3.9x9.9mm_P1.27mm, F.Cu at (144.9, 102.8)
- added U54: 74ACT151, Package_SO:SOIC-16_3.9x9.9mm_P1.27mm, F.Cu at (144.9, 78.8)
- added U55: 74ACT151, Package_SO:SOIC-16_3.9x9.9mm_P1.27mm, F.Cu at (145.1, 90.8)
- added U56: 74ACT151, Package_SO:SOIC-16_3.9x9.9mm_P1.27mm, F.Cu at (145.0, 66.8)
- moved C45 227.5 mm to (79.2, 61.7)
- moved C46 215.7 mm to (91.0, 79.8)
- moved C48 205.8 mm to (105.5, 86.6)
- moved C47 204.9 mm to (105.5, 74.6)
- moved U41 181.7 mm to (76.7, 68.1)
- moved U42 181.4 mm to (76.7, 80.1)
- moved U43 181.2 mm to (76.7, 92.1)
- moved U44 181.0 mm to (76.7, 104.1)
- moved U3 179.1 mm to (88.8, 85.8)
- moved U45 174.7 mm to (103.3, 68.6)
- moved U46 174.5 mm to (103.3, 80.6)
- moved U47 174.3 mm to (103.3, 92.6)
- moved U48 174.0 mm to (103.3, 104.6)
- moved C3 173.2 mm to (105.5, 62.6)
- moved C43 133.3 mm to (79.0, 98.1)
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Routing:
- added copper zone on In1.Cu, net GND
- added copper zone on In2.Cu, net VCC
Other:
- board outline added: 99.7 x 99.8 mm
- copper layers 2 -> 4

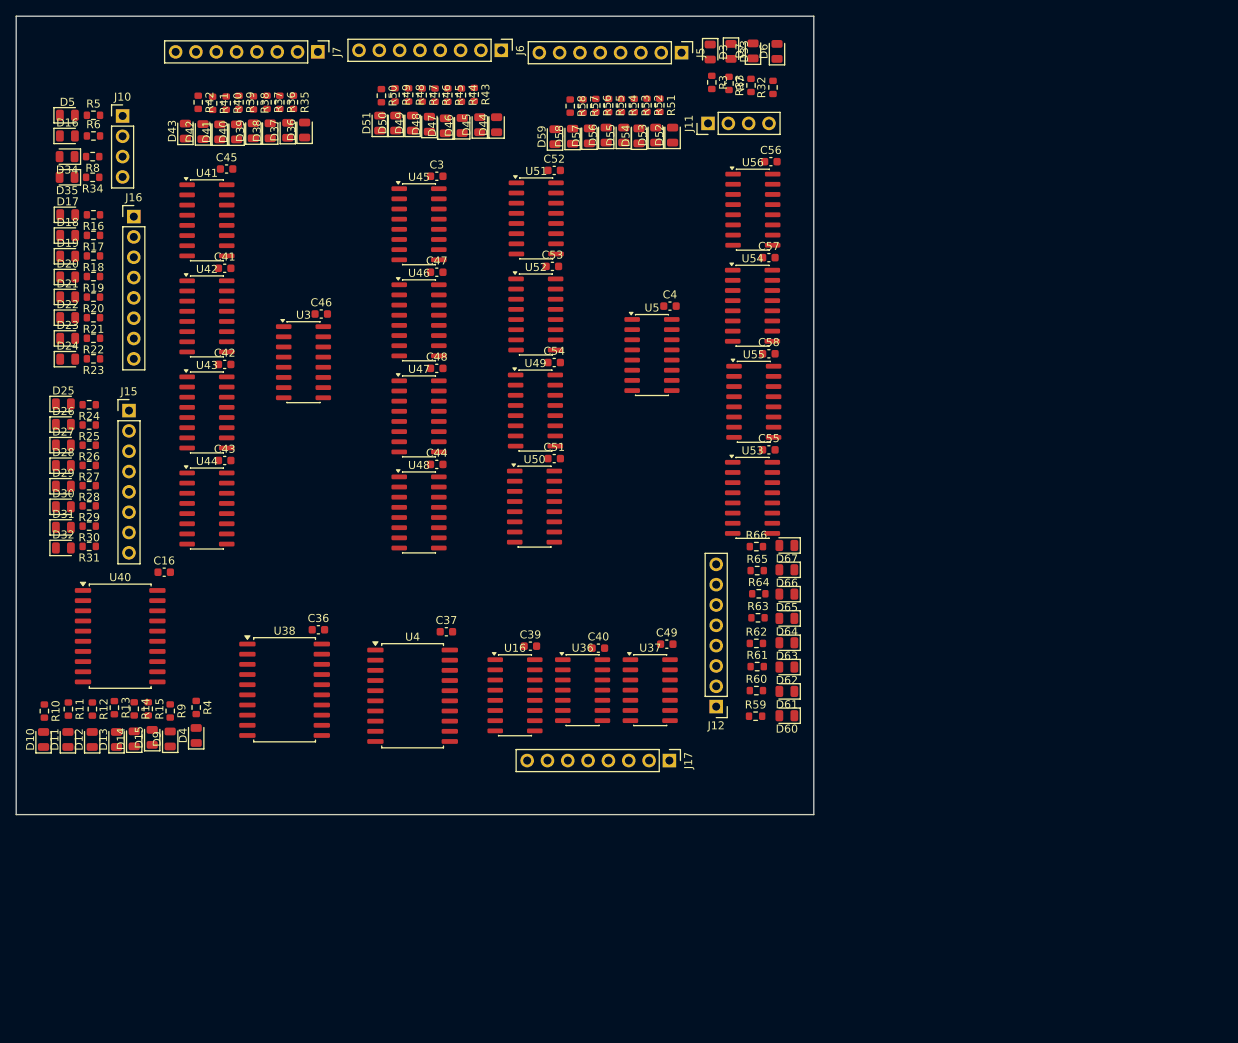
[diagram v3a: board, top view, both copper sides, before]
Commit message: feat: placed and routed opcode buses
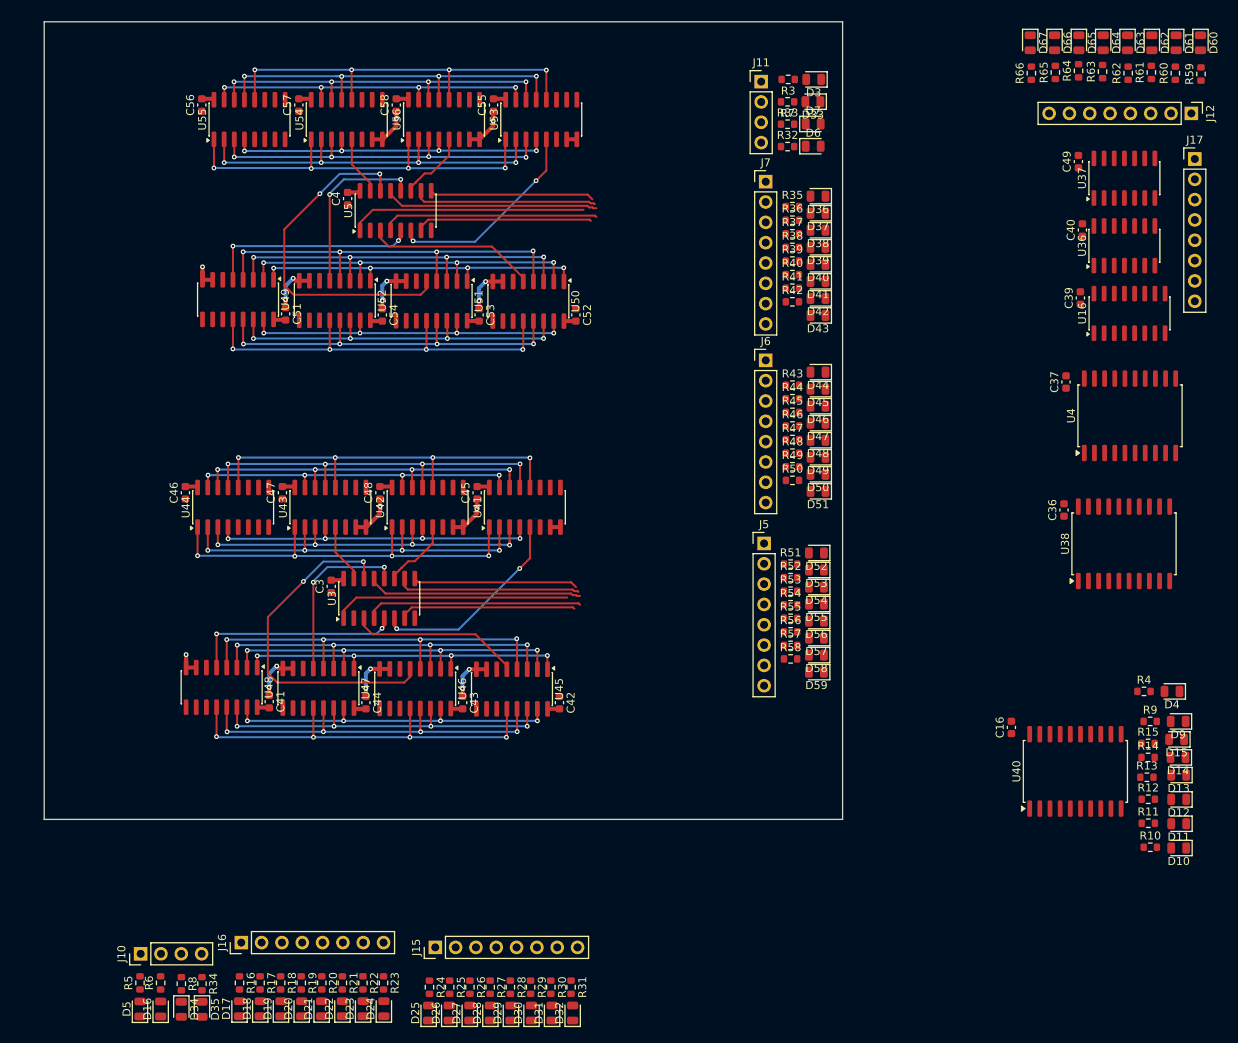
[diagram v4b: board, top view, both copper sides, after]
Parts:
- moved D10 142.5 mm to (198.2, 146.6), turned to 180 degrees
- moved R10 139.3 mm to (194.7, 146.5), turned to 0 degrees
- moved D11 139.2 mm to (198.2, 143.5), turned to 180 degrees
- moved D12 136.0 mm to (198.2, 140.5), turned to 180 degrees
- moved R11 135.7 mm to (194.4, 143.5), turned to 0 degrees
- moved D13 132.8 mm to (198.2, 137.5), turned to 180 degrees
- moved R12 132.5 mm to (194.4, 140.5), turned to 0 degrees
- moved D14 130.5 mm to (198.1, 135.2), turned to 180 degrees
- moved R13 129.4 mm to (194.2, 137.7), turned to 0 degrees
- moved D15 128.0 mm to (197.9, 133.0), turned to 180 degrees
- moved R14 126.9 mm to (194.4, 135.2), turned to 0 degrees
- moved D9 126.0 mm to (198.1, 130.8), turned to 180 degrees
- moved R15 125.1 mm to (194.4, 133.5), turned to 0 degrees
- moved R9 122.5 mm to (194.6, 130.8), turned to 0 degrees
- moved D4 122.1 mm to (197.4, 127.0), turned to 180 degrees
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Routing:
- net ALU_OPCODE_Y7: track 0.00 -> 102.8 mm, vias 0 -> 8
- net ALU_OPCODE_Y3: track 0.00 -> 101.8 mm, vias 0 -> 8
- net ALU_OPCODE_X0: track 0.00 -> 101.8 mm, vias 0 -> 8
- net ALU_OPCODE_X7: track 0.00 -> 101.6 mm, vias 0 -> 8
- net ALU_OPCODE_Y6: track 0.00 -> 97.8 mm, vias 0 -> 8
- net ALU_OPCODE_X6: track 0.00 -> 96.2 mm, vias 0 -> 8
- net ALU_OPCODE_X1: track 0.00 -> 96.2 mm, vias 0 -> 8
- net ALU_OPCODE_Y2: track 0.00 -> 96.2 mm, vias 0 -> 8
- net ALU_OPCODE_Y5: track 0.00 -> 91.0 mm, vias 0 -> 8
- net ALU_OPCODE_X2: track 0.00 -> 90.8 mm, vias 0 -> 8
- net ALU_OPCODE_X5: track 0.00 -> 90.8 mm, vias 0 -> 8
- net ALU_OPCODE_Y1: track 0.00 -> 90.7 mm, vias 0 -> 8
- net ALU_OPCODE_X3: track 0.00 -> 85.6 mm, vias 0 -> 8
- net ALU_OPCODE_X4: track 0.00 -> 85.3 mm, vias 0 -> 8
- net ALU_OPCODE_Y4: track 0.00 -> 85.2 mm, vias 0 -> 8
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- removed copper zone on In1.Cu, net GND
- removed copper zone on In2.Cu, net VCC
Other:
- board size 99.7 x 99.8 mm -> 99.8 x 99.7 mm
- copper layers 4 -> 2
